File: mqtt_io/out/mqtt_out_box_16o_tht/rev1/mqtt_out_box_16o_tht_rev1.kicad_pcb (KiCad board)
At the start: 2 copper layers, 142.8 x 171.9 mm, 139 parts, among them J1 Conn_01x04_Pin, J18 Conn_01x04_Pin, J19 Conn_01x02_Pin, K1 FINDER-40.31, K10 FINDER-40.31, K11 FINDER-40.31, K12 FINDER-40.31, K13 FINDER-40.31, K14 FINDER-40.31, K15 FINDER-40.31, K16 FINDER-40.31, K2 FINDER-40.31, K3 FINDER-40.31, K4 FINDER-40.31, K5 FINDER-40.31, K6 FINDER-40.31, K7 FINDER-40.31, K8 FINDER-40.31, K9 FINDER-40.31, Q1 IRFZ24N, Q10 IRFZ24N, Q11 IRFZ24N, Q12 IRFZ24N, Q13 IRFZ24N, Q14 IRFZ24N, Q15 IRFZ24N, Q16 IRFZ24N, Q2 IRFZ24N, Q3 IRFZ24N, Q4 IRFZ24N, Q5 IRFZ24N, Q6 IRFZ24N, Q7 IRFZ24N, Q8 IRFZ24N, Q9 IRFZ24N, U1 MCP23017_SP

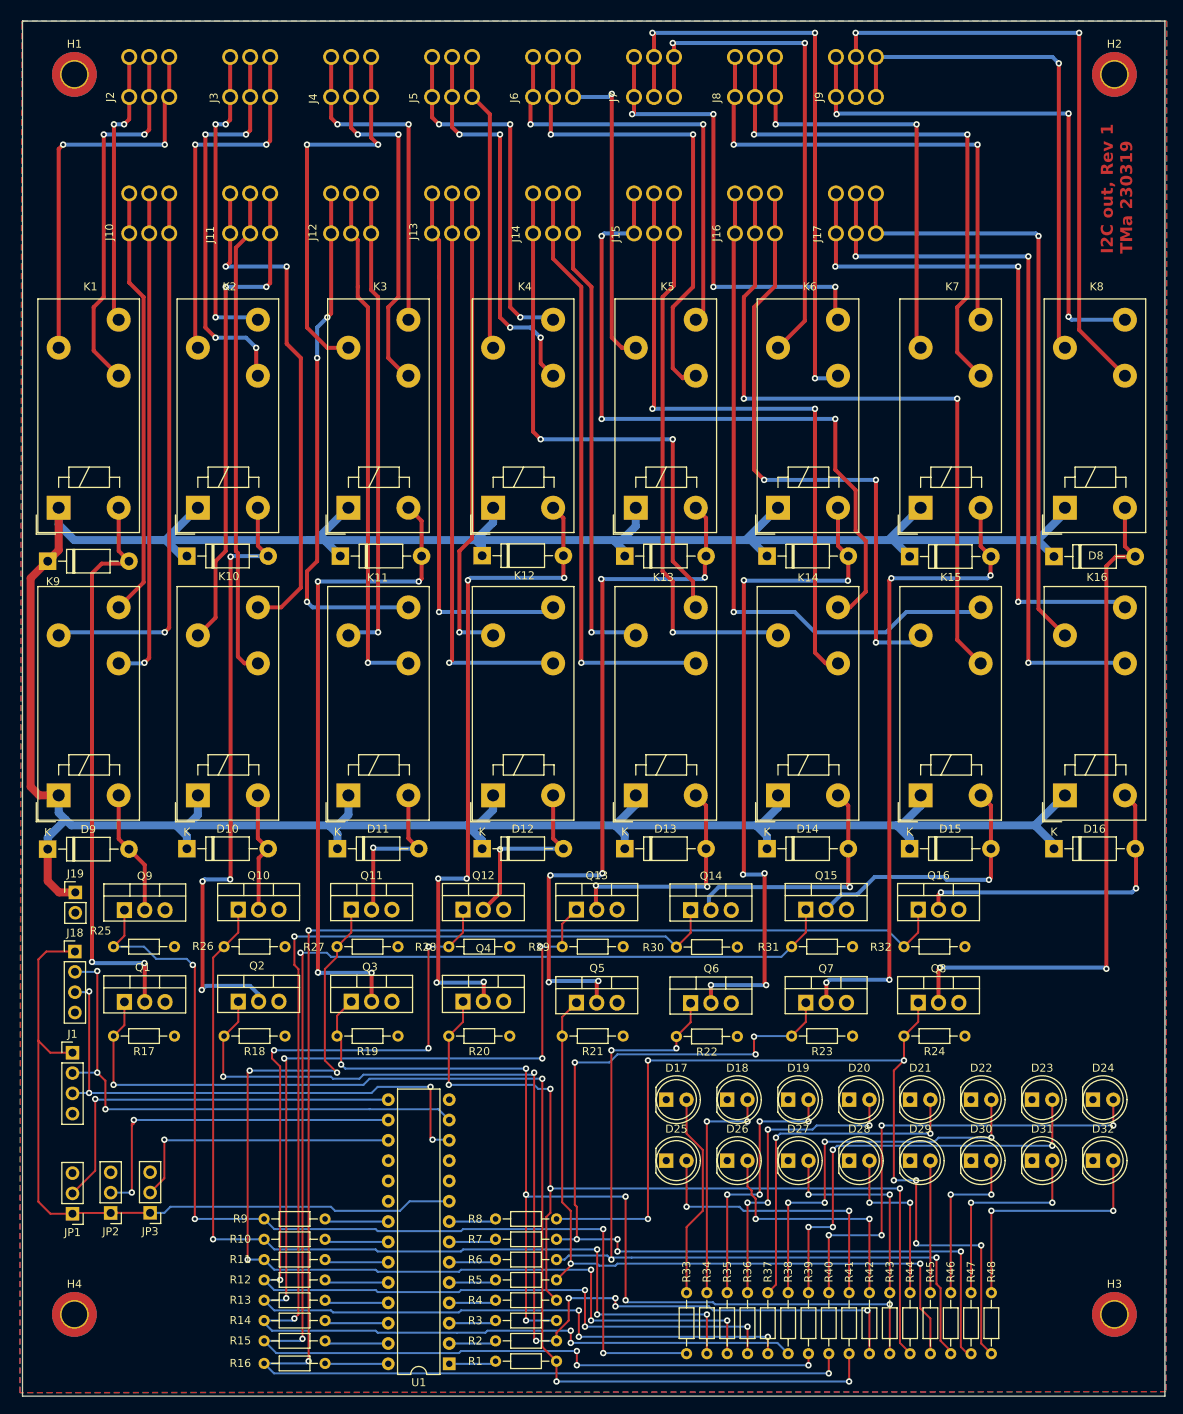
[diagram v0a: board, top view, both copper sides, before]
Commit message: Pullup für ic2 eingefügt (4k7)
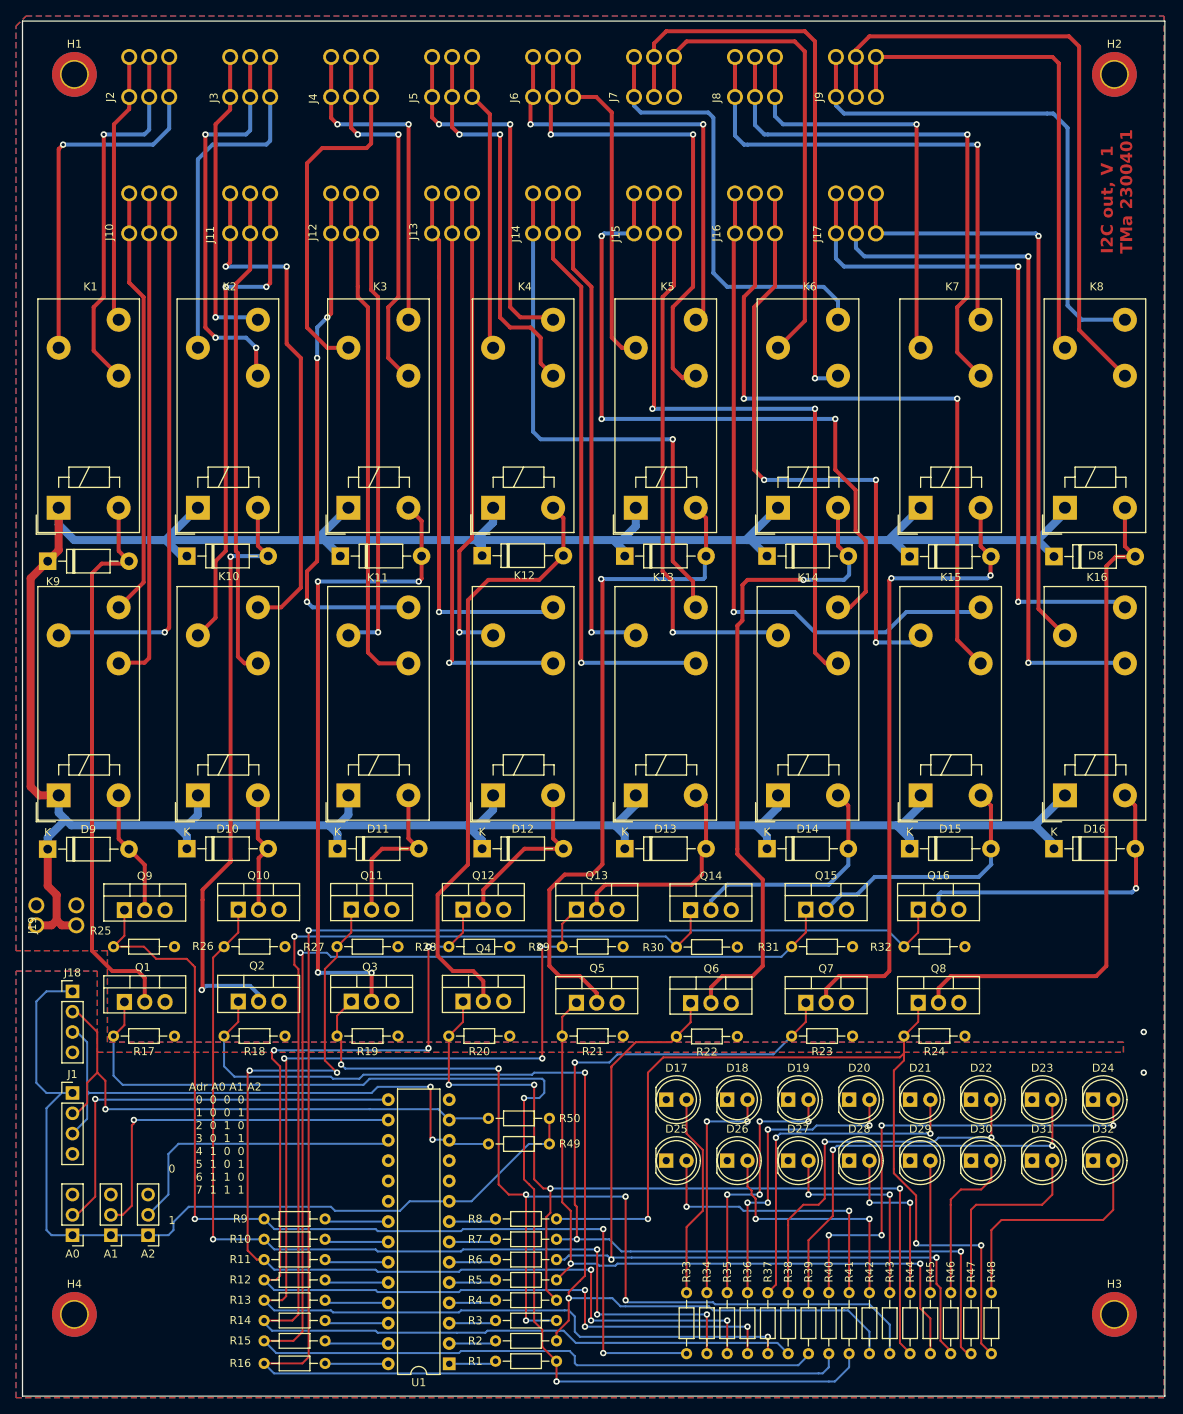
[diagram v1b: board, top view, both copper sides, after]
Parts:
- removed JP1, JP2, JP3: Jumper_3_Open, Connector_PinHeader_2.54mm:PinHeader_1x03_P2.54mm_Vertical
- added A0: Jumper_3_Open, Connector_PinHeader_2.54mm:PinHeader_1x03_P2.54mm_Vertical, F.Cu at (19.8, 165.1)
- added A1: Jumper_3_Open, Connector_PinHeader_2.54mm:PinHeader_1x03_P2.54mm_Vertical, F.Cu at (24.6, 165.1)
- added A2: Jumper_3_Open, Connector_PinHeader_2.54mm:PinHeader_1x03_P2.54mm_Vertical, F.Cu at (29.2, 165.1)
- added R49: 100R, Resistor_THT:R_Axial_DIN0204_L3.6mm_D1.6mm_P7.62mm_Horizontal, F.Cu at (71.8, 153.7)
- added R50: 100R, Resistor_THT:R_Axial_DIN0204_L3.6mm_D1.6mm_P7.62mm_Horizontal, F.Cu at (71.8, 150.5)
- J19: value Conn_01x02_Pin -> ~; footprint Connector_PinHeader_2.54mm:PinHeader_1x02_P2.54mm_Vertical -> parts_tma_1:AST_041-2
- moved J19 6.38 mm to (15.2, 126.4), turned to 90 degrees
- moved J1 5.03 mm to (19.8, 147.3)
- moved J18 4.99 mm to (19.8, 134.6)
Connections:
- net +5V renamed VDD
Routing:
- net VDD: track 93.2 -> 111.6 mm
- net Net-(D4-A): track 83.9 -> 76.4 mm, vias 6 -> 0
- net VCC: track 422.7 -> 429.5 mm
- net Net-(D5-A): track 88.3 -> 83.9 mm, vias 6 -> 1
- net Net-(D6-A): track 85.5 -> 81.6 mm, vias 6 -> 1
- net /b1: track 135.7 -> 132.0 mm, vias 7 -> 2
- net Net-(J1-Pin_3): track 68.4 -> 71.9 mm, vias 4 -> 2
- net Net-(J7-Pad1): track 58.5 -> 55.4 mm, vias 4 -> 0
- net /AD0: track 49.6 -> 52.6 mm
- net Net-(J4-Pad3): track 49.3 -> 46.6 mm, vias 2 -> 0
- net Net-(J9-Pad2): track 81.2 -> 78.5 mm, vias 2 -> 0
- net Net-(D14-A): track 32.0 -> 29.4 mm, vias 1 -> 0
- net Net-(J9-Pad1): track 68.8 -> 66.3 mm, vias 3 -> 0
- net /b6: track 122.8 -> 120.3 mm, vias 7 -> 3
- net Net-(D13-A): track 29.1 -> 26.8 mm, vias 2 -> 0
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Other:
- board text added: "0 1"
- board text added: "Adr A0 A1 A2 0 0 0 0 1 0 0 1 2 0 1 0 3 0 1 1 4 1 0 0 5 1 0 1 6 1 1 0 7 1 1 1"
- board text added: "I2C out, V 1 TMa 2300401"
- board text removed: "I2C out, Rev 1 TMa 230319"

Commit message: neue Dateien eingefügt.
out Platine rev 2, testprogramm für pi pico
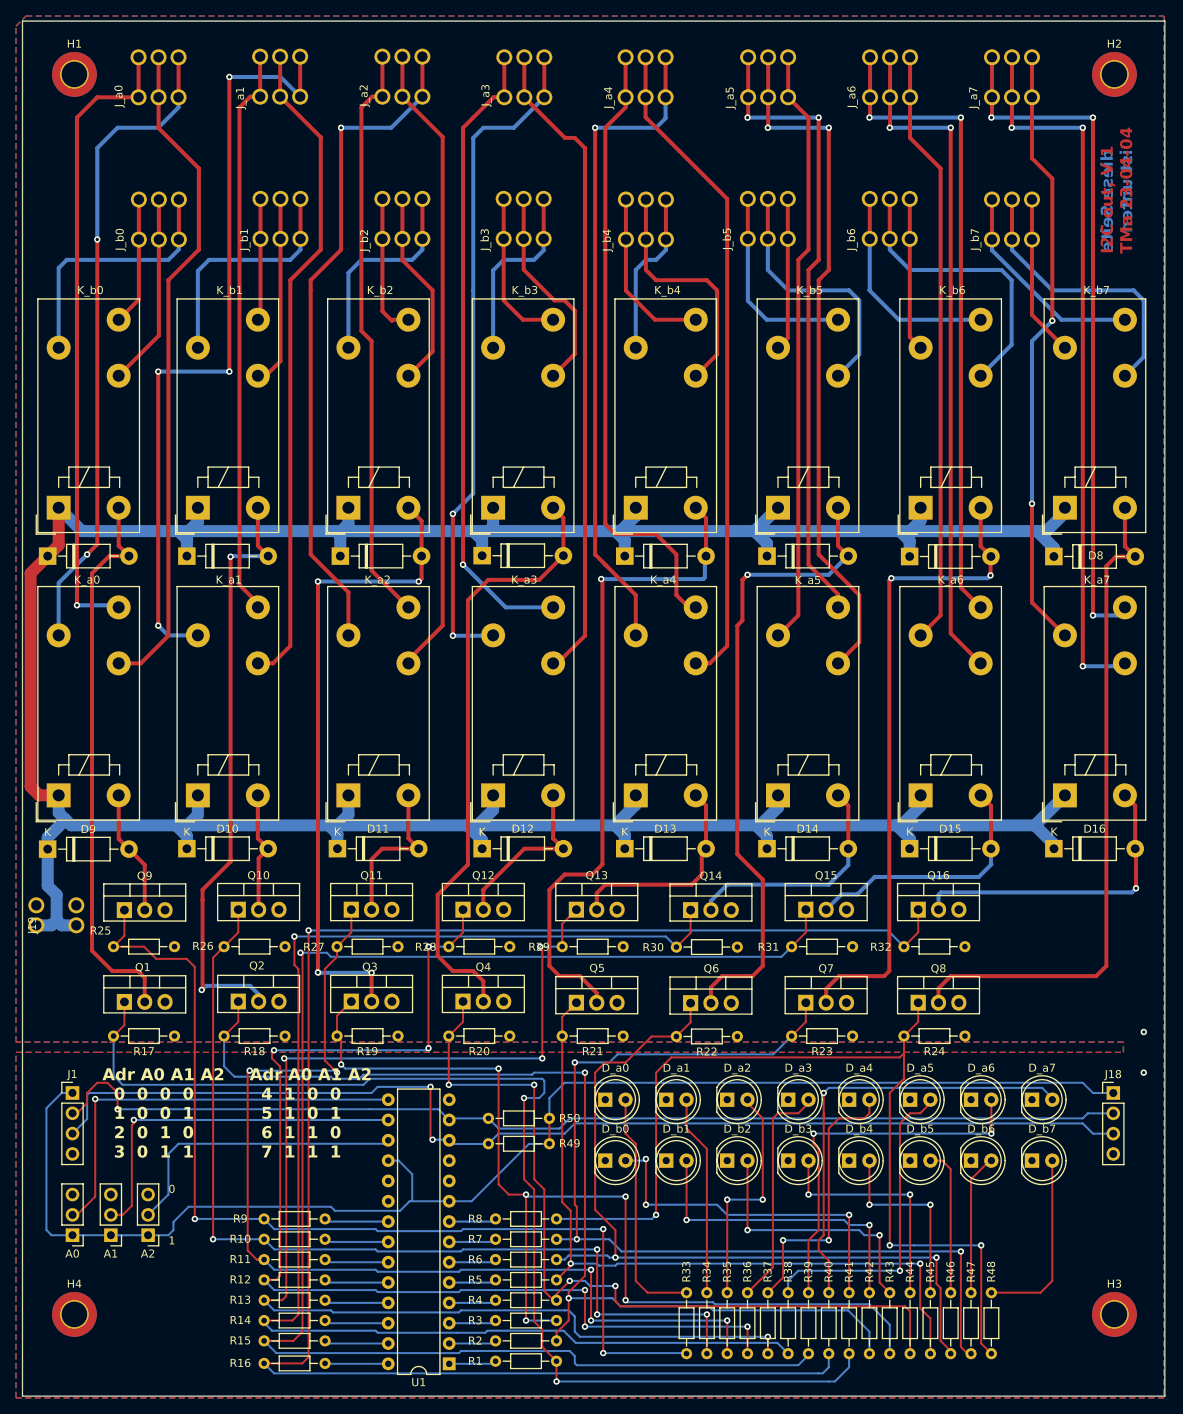
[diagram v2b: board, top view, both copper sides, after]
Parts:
- R49, R50: value 100R -> 4k7
- moved J18 130.7 mm to (149.9, 147.3)
- moved J_b7 26.4 mm to (134.7, 40.6)
- moved J_a7 25.9 mm to (134.7, 22.9)
- moved J_b6 24.5 mm to (119.4, 40.6)
- moved J_a6 24.0 mm to (119.5, 22.9)
- moved J_b5 22.7 mm to (104.2, 40.6)
- moved J_a5 22.2 mm to (104.2, 22.9)
- moved J_b4 21.3 mm to (88.9, 40.6)
- moved J_a4 20.6 mm to (88.9, 22.9)
- moved J_b3 19.9 mm to (73.7, 40.6)
- moved J_a3 19.3 mm to (73.7, 22.9)
- moved J_b2 18.9 mm to (58.5, 40.6)
- moved J_a2 18.3 mm to (58.5, 22.8)
- moved J_b1 18.1 mm to (43.3, 40.6)
- moved J_b0 17.9 mm to (28.1, 40.6)
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- renumbered D17 to D_a0, D18 to D_a1, D19 to D_a2, D20 to D_a3, D21 to D_a4, D22 to D_a5, D23 to D_a6, D24 to D_a7, D25 to D_b0, D26 to D_b1, D27 to D_b2, D28 to D_b3, D29 to D_b4, D30 to D_b5, D31 to D_b6, D32 to D_b7, J10 to J_a0, J11 to J_a1, J12 to J_a2, J13 to J_a3, J14 to J_a4, J15 to J_a5, J16 to J_a6, J17 to J_a7, J2 to J_b0, J3 to J_b1, J4 to J_b2, J5 to J_b3, J6 to J_b4, J7 to J_b5, J8 to J_b6, J9 to J_b7, K9 to K_a0, K10 to K_a1, K11 to K_a2, K12 to K_a3, K13 to K_a4, K14 to K_a5, K15 to K_a6, K16 to K_a7, K1 to K_b0, K2 to K_b1, K3 to K_b2, K4 to K_b3, K5 to K_b4, K6 to K_b5, K7 to K_b6, K8 to K_b7
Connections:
- U1 pad 18: GND -> VDD
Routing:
- net Net-(J1-Pin_3): track 71.9 -> 142.5 mm
- net Net-(J1-Pin_2): track 69.4 -> 136.9 mm
- net VDD: track 111.6 -> 172.6 mm
- net Net-(J_b7-Pad3): track 64.1 -> 20.2 mm
- net Net-(J_b7-Pad2): track 78.5 -> 35.8 mm
- net Net-(J_b5-Pad3): track 61.3 -> 19.1 mm
- net Net-(J_b5-Pad2): track 73.1 -> 32.4 mm, vias 1 -> 0
- net Net-(J_b7-Pad1): track 66.3 -> 26.6 mm
- net Net-(J_a1-Pad3): track 62.0 -> 97.8 mm, vias 2 -> 4
- net Net-(J_b6-Pad1): track 62.7 -> 26.9 mm, vias 1 -> 0
- net Net-(J_b6-Pad3): track 53.7 -> 19.2 mm, vias 1 -> 0
- net Net-(J_b4-Pad1): track 55.0 -> 21.6 mm, vias 2 -> 0
- net Net-(J_b4-Pad2): track 61.4 -> 30.5 mm, vias 2 -> 0
- net Net-(J_b6-Pad2): track 67.4 -> 36.7 mm, vias 1 -> 0
- net Net-(J_b5-Pad1): track 55.4 -> 25.0 mm
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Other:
- board text added: "Adr A0 A1 A2 0 0 0 0 1 0 0 1 2 0 1 0 3 0 1 1"
- board text added: "Adr A0 A1 A2 4 1 0 0 5 1 0 1 6 1 1 0 7 1 1 1"
- board text added: "I2C out, V 1 TMa 23-04-04"
- board text added: "diese Seite ist unten"
- board text removed: "Adr A0 A1 A2 0 0 0 0 1 0 0 1 2 0 1 0 3 0 1 1 4 1 0 0 5 1 0 1 6 1 1 0 7 1 1 1"
- board text removed: "I2C out, V 1 TMa 2300401"
